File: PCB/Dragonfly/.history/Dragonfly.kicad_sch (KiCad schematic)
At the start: 16 parts, among them SW1 SW_SPST, SW2 SW_SPST, U1 STM32F405RGTx, X1 TSX-3225

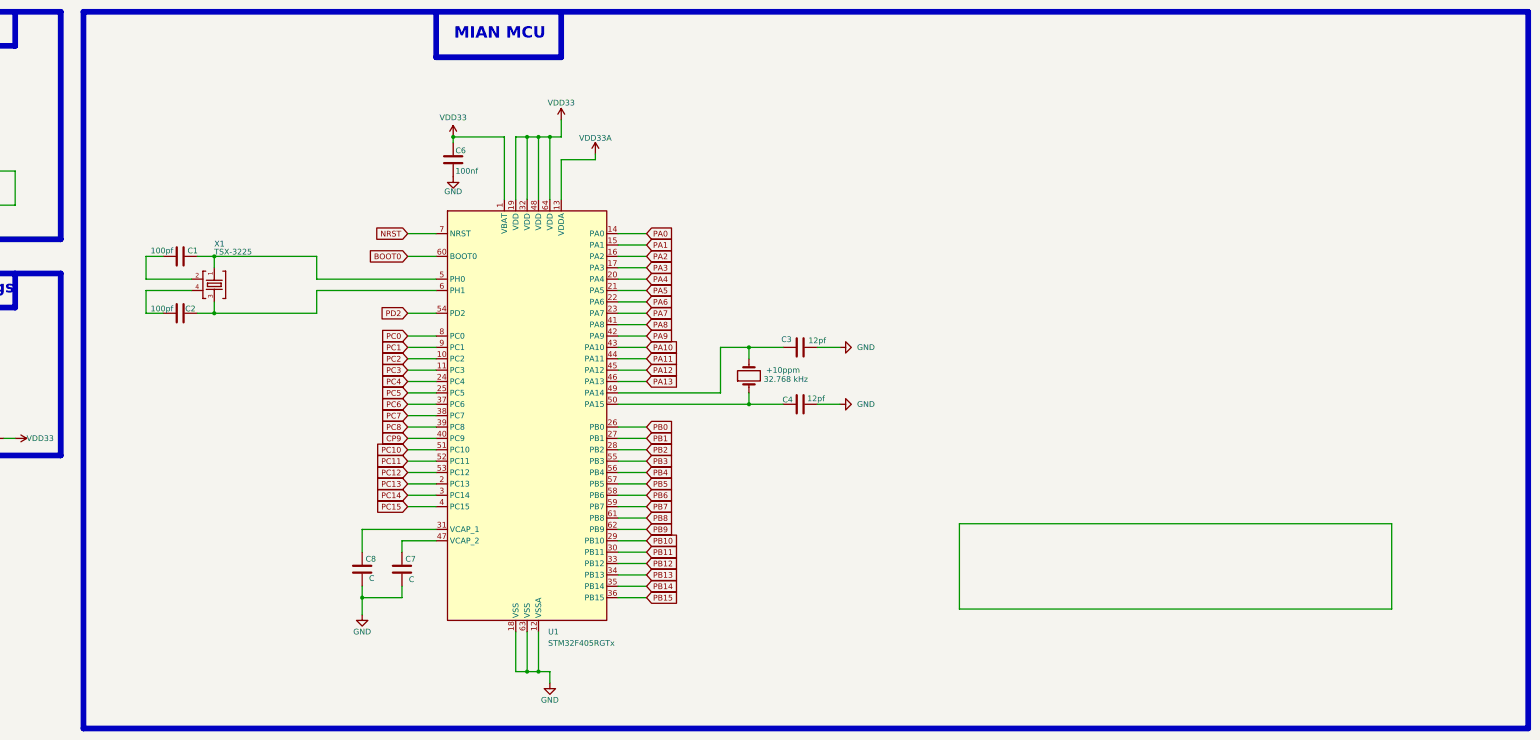
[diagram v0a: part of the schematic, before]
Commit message: Update Dragonfly.kicad_sch
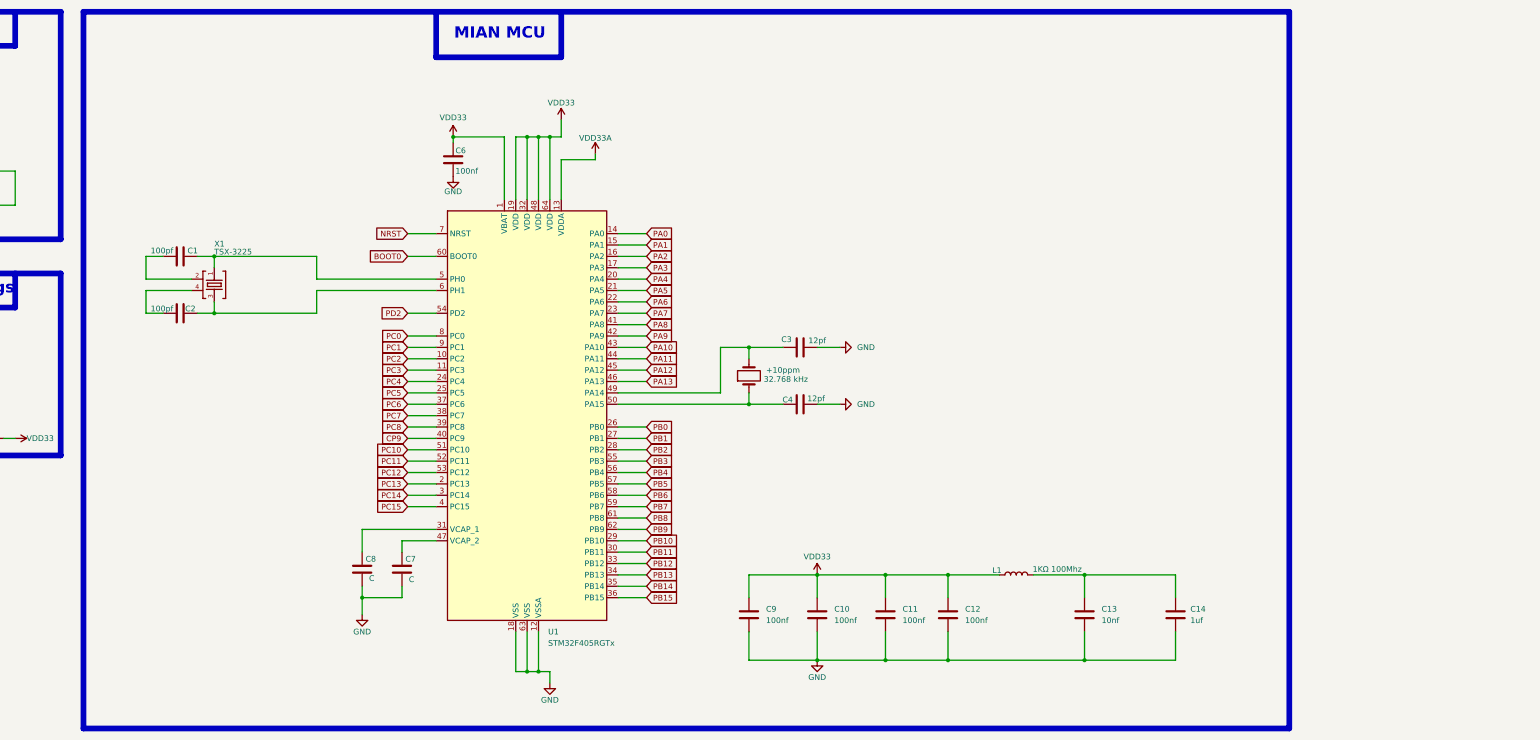
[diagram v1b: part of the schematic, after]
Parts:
- added C10, C11, C12, C9: 100nf, symbol Device:C
- added C13: 10nf, symbol Device:C
- added C14: 1uf, symbol Device:C
- added L1: 1KΩ 100Mhz, symbol Device:L
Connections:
- net GND: now also C10.2, C11.2, C12.2, C13.2, C14.2, C9.2
- net VDD33: now also C10.1, C11.1, C12.1, C9.1, L1.1
- new net: C13.1, C14.1, L1.2

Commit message: Update Dragonfly.kicad_sch
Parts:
- added D1, D2: D, symbol Device:D
- added R4, R5: 5.1kΩ, symbol Device:R
- C1, C2: value 100pf -> 10pf
- C7, C8: value C -> 2.2uF
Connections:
- net GND: now also D1.2 (A), D2.2 (A)
- net PB2: now also R4.1
- net VDD33: now also R5.1
- new net: D1.1 (K), R4.2
- new net: D2.1 (K), R5.2
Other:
- note added: "Indicator light"

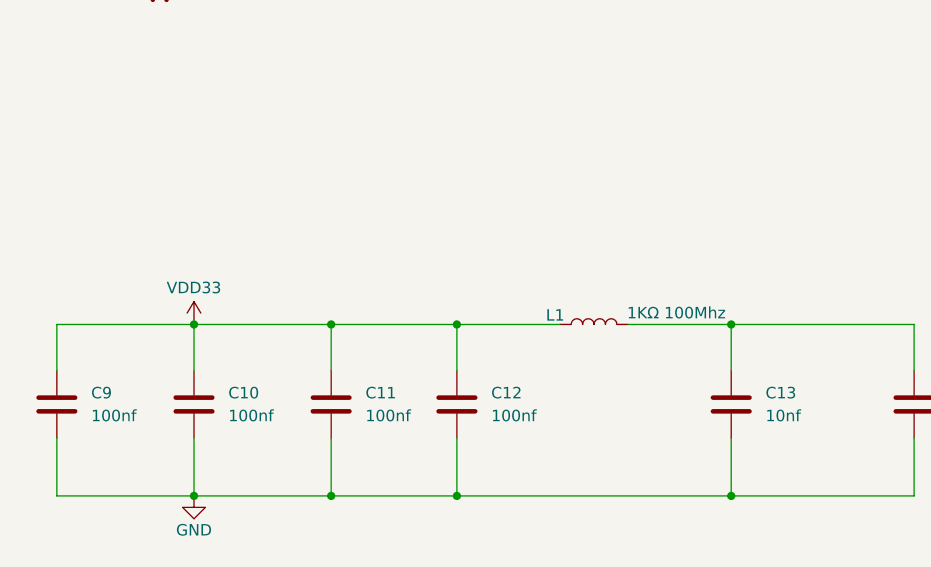
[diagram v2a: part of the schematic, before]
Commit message: Update Dragonfly.kicad_sch
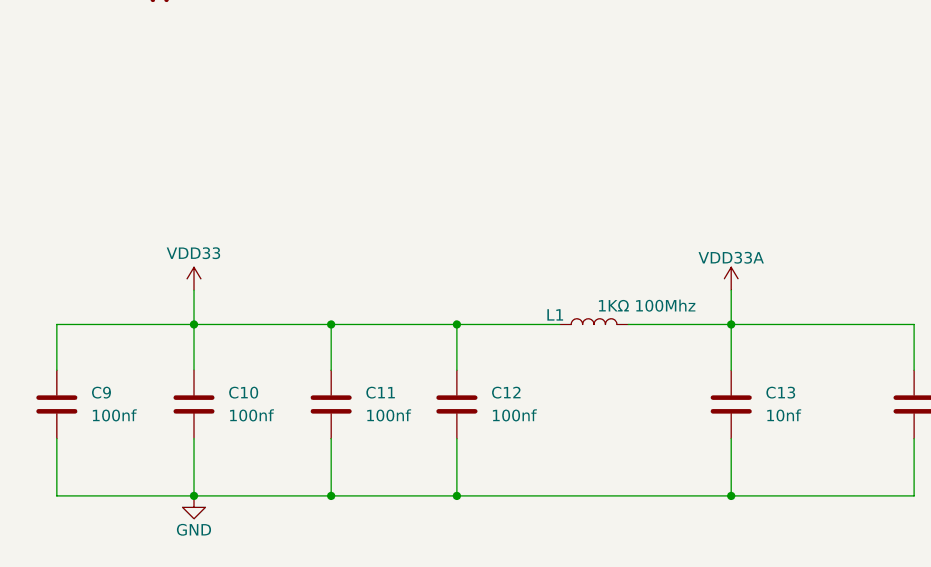
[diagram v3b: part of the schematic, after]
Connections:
- net VDD33A: now also C13.1, C14.1, L1.2
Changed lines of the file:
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@@
 	(wire
 		(pts
+			(xy 688.34 144.78) (xy 688.34 148.59)
+		)
+		(stroke
+			(width 0)
+			(type default)
+		)
+	)
+	(wire
+		(pts
 			(xy 584.2 90.17) (xy 590.55 90.17)
 		)
@@
 	(wire
 		(pts
+			(xy 628.65 144.78) (xy 628.65 148.59)
+		)
+		(stroke
+			(width 0)
+			(type default)
+		)
+	)
+	(wire
+		(pts
 			(xy 613.41 97.79) (xy 621.03 97.79)
 		)
@@
 	)
 	(symbol
+		(lib_id "power:VDD")
+		(at 688.34 144.78 0)
+		(unit 1)
+		(body_style 1)
+		(exclude_from_sim no)
+		(in_bom yes)
+		(on_board yes)
+		(in_pos_files yes)
+		(dnp no)
+		(property "Reference" "#PWR018"
+			(at 688.34 148.59 0)
+			(hide yes)
+			(show_name no)
+			(do_not_autoplace no)
+			(effects
+				(font
+					(size 1.27 1.27)
+				)
+			)
+		)
+		(property "Value" "VDD33A"
+			(at 688.34 141.224 0)
+			(show_name no)
+			(do_not_autoplace no)
+			(effects
+				(font
+					(size 1.27 1.27)
+				)
+			)
+		)
+		(property "Footprint" ""
+			(at 688.34 144.78 0)
+			(hide yes)
+			(show_name no)
+			(do_not_autoplace no)
+			(effects
+				(font
+					(size 1.27 1.27)
+				)
+			)
+		)
+		(property "Datasheet" ""
+			(at 688.34 144.78 0)
+			(hide yes)
+			(show_name no)
+			(do_not_autoplace no)
+			(effects
+				(font
+					(size 1.27 1.27)
+				)
+			)
+		)
+		(property "Description" "Power symbol creates a global label with name \"VDD\""
+			(at 688.34 144.78 0)
+			(hide yes)
+			(show_name no)
+			(do_not_autoplace no)
+			(effects
+				(font
+					(size 1.27 1.27)
+				)
+			)
+		)
+		(pin "1"
+		)
+		(instances
+			(project "Dragonfly"
+				(path "/f0708a7e-abc5-4571-a850-719a309c37b6"
+					(reference "#PWR018")
+					(unit 1)
+				)
+			)
+		)
+	)
+	(symbol
 		(lib_id "Device:R")
 		(at 773.43 63.5 90)
@@
 	(symbol
 		(lib_id "power:VDD")
-		(at 628.65 148.59 0)
+		(at 628.65 144.78 0)
 		(unit 1)
 		(body_style 1)
@@
 		(dnp no)
 		(property "Reference" "#PWR013"
-			(at 628.65 152.4 0)
+			(at 628.65 148.59 0)
 			(hide yes)
 			(show_name no)
@@
 		)
 		(property "Value" "VDD33"
-			(at 628.65 144.526 0)
+			(at 628.65 140.716 0)
 			(show_name no)
 			(do_not_autoplace no)
@@
 		)
 		(property "Footprint" ""
-			(at 628.65 148.59 0)
+			(at 628.65 144.78 0)
 			(hide yes)
 			(show_name no)
@@
 		)
 		(property "Datasheet" ""
-			(at 628.65 148.59 0)
+			(at 628.65 144.78 0)
 			(hide yes)
 			(show_name no)
@@
 		)
 		(property "Description" "Power symbol creates a global label with name \"VDD\""
-			(at 628.65 148.59 0)
+			(at 628.65 144.78 0)
 			(hide yes)
 			(show_name no)
@@
 		)
 		(property "Value" "1KΩ 100Mhz"
-			(at 682.244 147.32 90)
+			(at 678.942 146.558 90)
 			(show_name no)
 			(do_not_autoplace no)

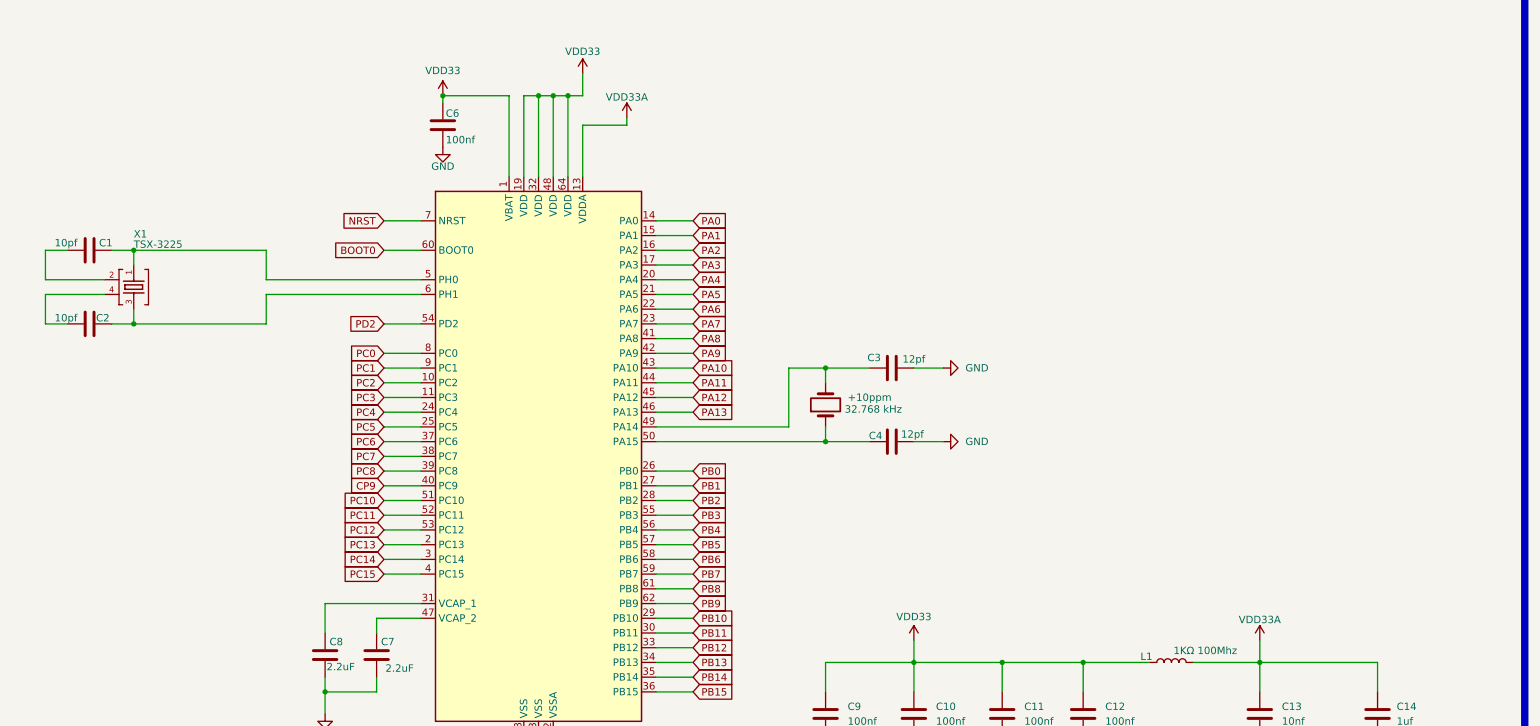
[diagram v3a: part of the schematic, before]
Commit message: Update Dragonfly.kicad_sch
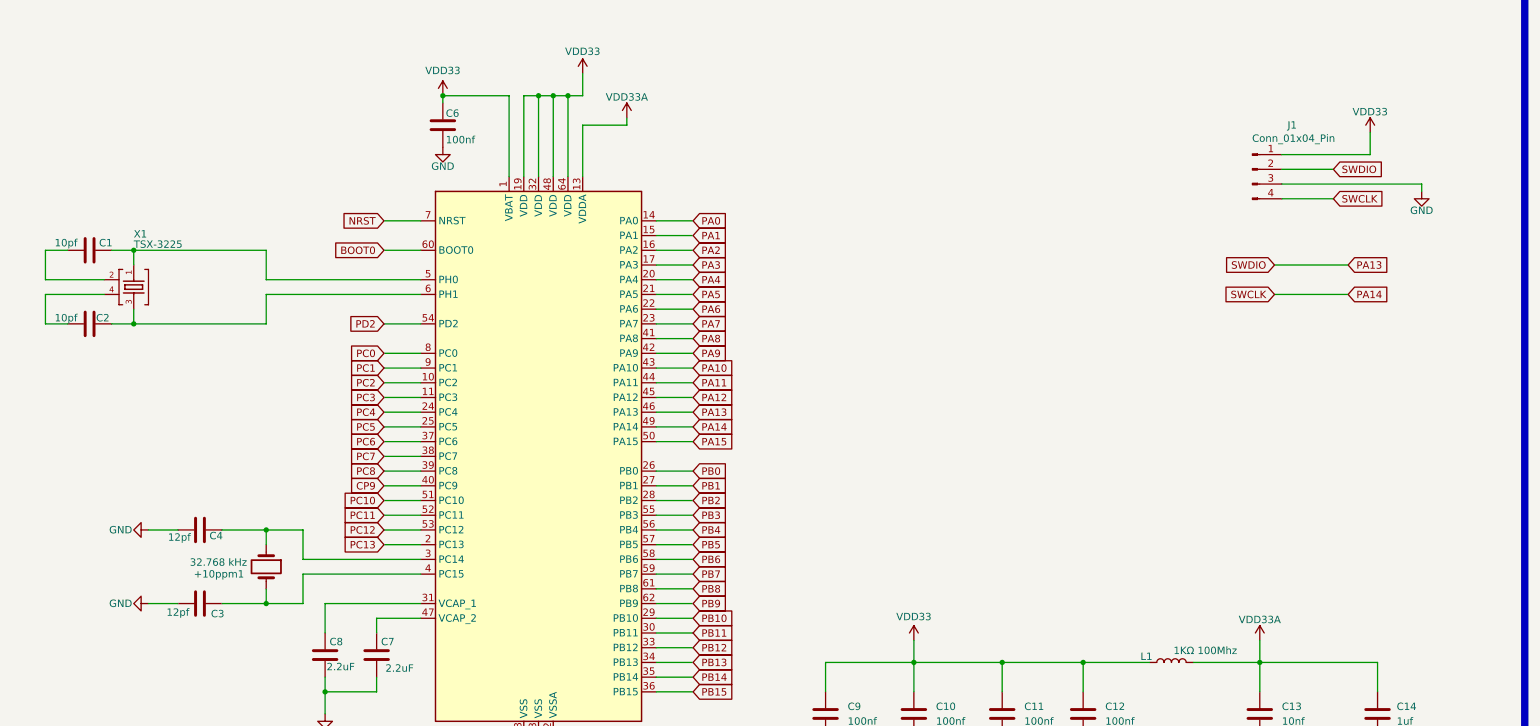
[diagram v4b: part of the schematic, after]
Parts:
- removed +10ppm: 32.768 kHz, symbol Device:Crystal
- added +10ppm1: 32.768 kHz, symbol Device:Crystal
- added J1: Conn_01x04_Pin, symbol Connector:Conn_01x04_Pin
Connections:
- net PC14 is gone; now on an unnamed net: U1.3 (PC14)
- net PC15 is gone; now on an unnamed net: U1.4 (PC15)
- net GND: now also J1.3 (Pin_3)
- net PA13: now also J1.2 (Pin_2)
- net VDD33: now also J1.1 (Pin_1)
- net at C4.1: now also +10ppm1.1; no longer U1.50 (PA15)
- net at C3.1: now also +10ppm1.2; no longer U1.49 (PA14)
- new net PA14: J1.4 (Pin_4), U1.49 (PA14)
- new net PA15: U1.50 (PA15)

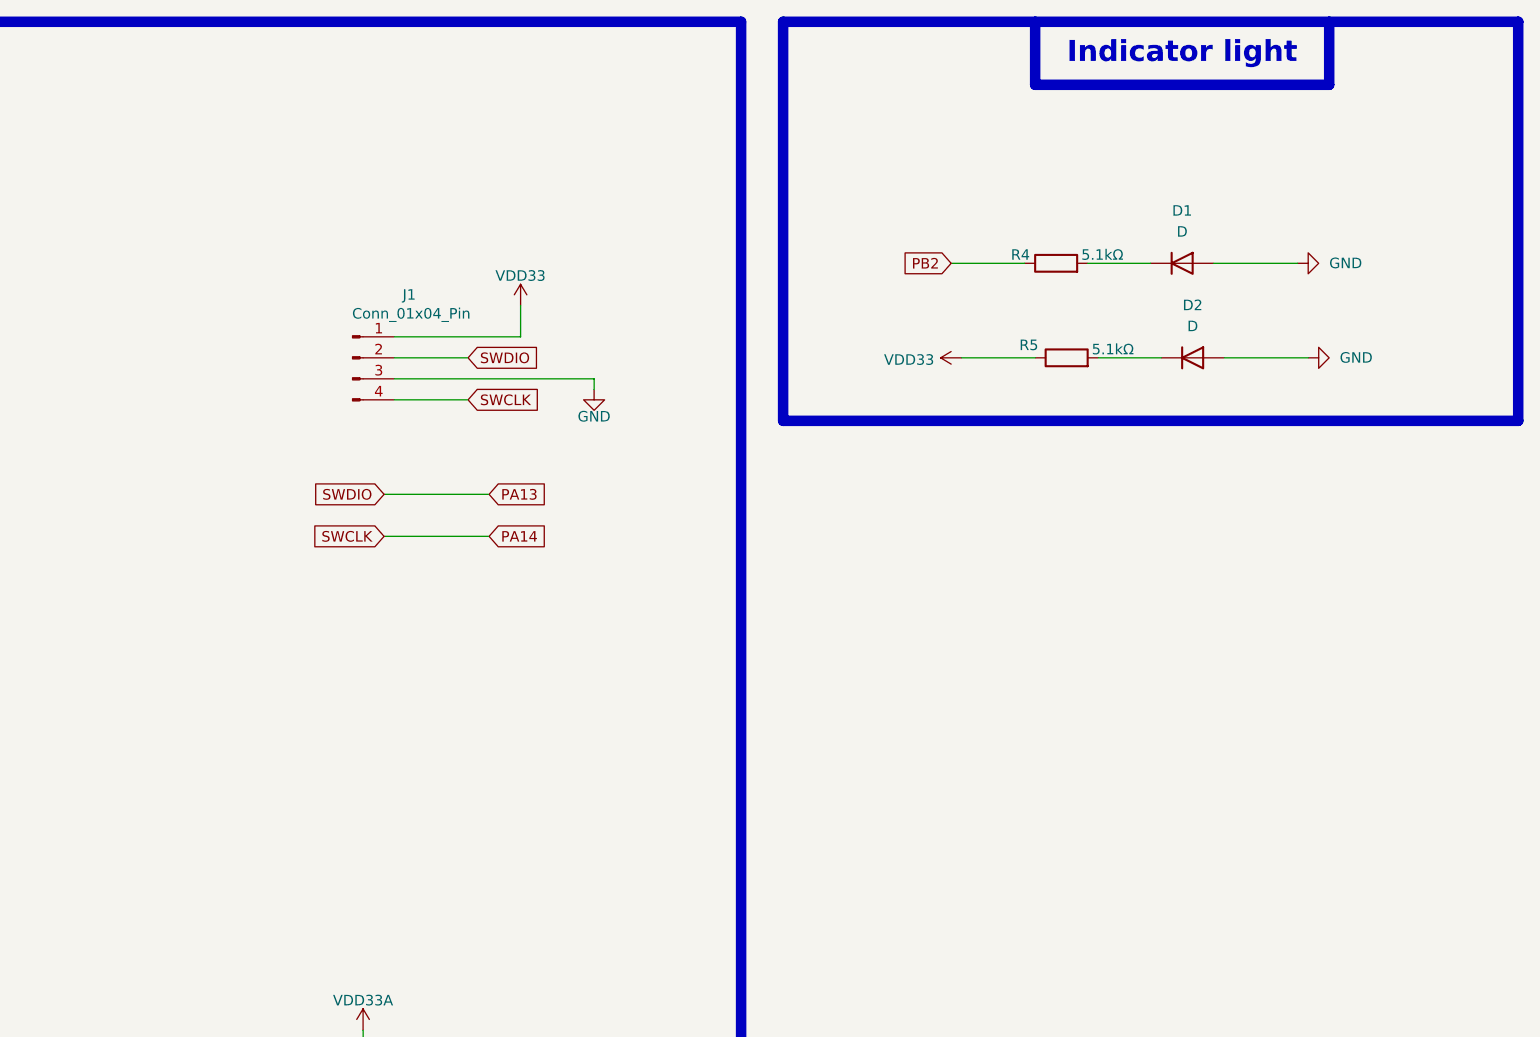
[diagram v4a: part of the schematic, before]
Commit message: Update Dragonfly.kicad_sch
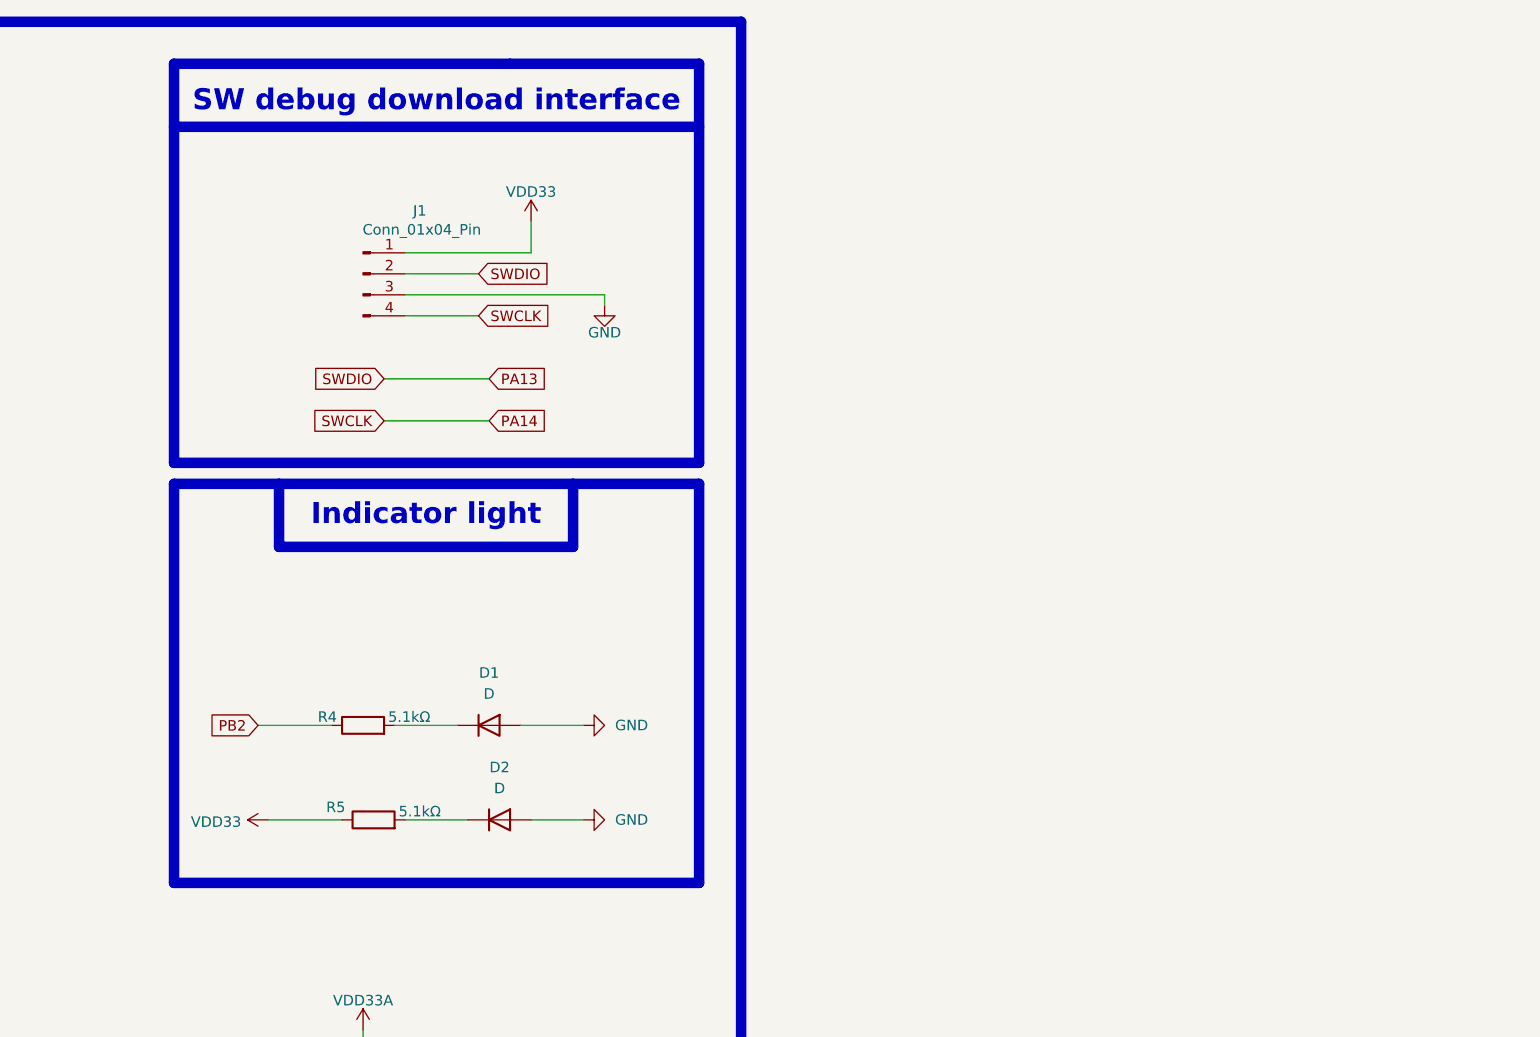
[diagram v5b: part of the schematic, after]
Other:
- note added: "SW debug download interface"
- moved on the sheet: D1, D2, J1, R4, R5
